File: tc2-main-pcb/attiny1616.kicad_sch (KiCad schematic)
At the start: 16 parts, among them SW2 K2-6639SP-M4SC-04, U1 ATtiny1616-M

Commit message: v0.4.0
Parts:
- removed SW2: K2-6639SP-M4SC-04, cacophony-library:KEY-SMD_4P-L6.0-W6.0-P3.90_K2-6639SP-K4SC-04, symbol cacophony-library:K2-6639SP-O4SC-04
- added SW1: SW_Push, Button_Switch_THT:SW_PUSH_6mm, symbol Switch:SW_Push
- LED1: LCSC (none) -> C2874115; LCSC Part C2874115 -> (none)
- renumbered C56 to C44, R49 to R40, R15 to R46
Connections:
- net ATtiny_SW: now also SW1.1
- net GND: now also SW1.2
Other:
- note added: "140uA when in set_sleep_mode(SLEEP_MODE_PWR_DOWN);"
- note added: "I2C Address 0x25"

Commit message: Small update for v0.4.1
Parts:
- SW1: LCSC (none) -> C4364951
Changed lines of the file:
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@@
+			)
+		)
+		(property "LCSC" "C4364951"
+			(at 204.47 116.84 0)
+			(effects
+				(font
+					(size 1.27 1.27)
+				)
+				(hide yes)
 			)
 		)

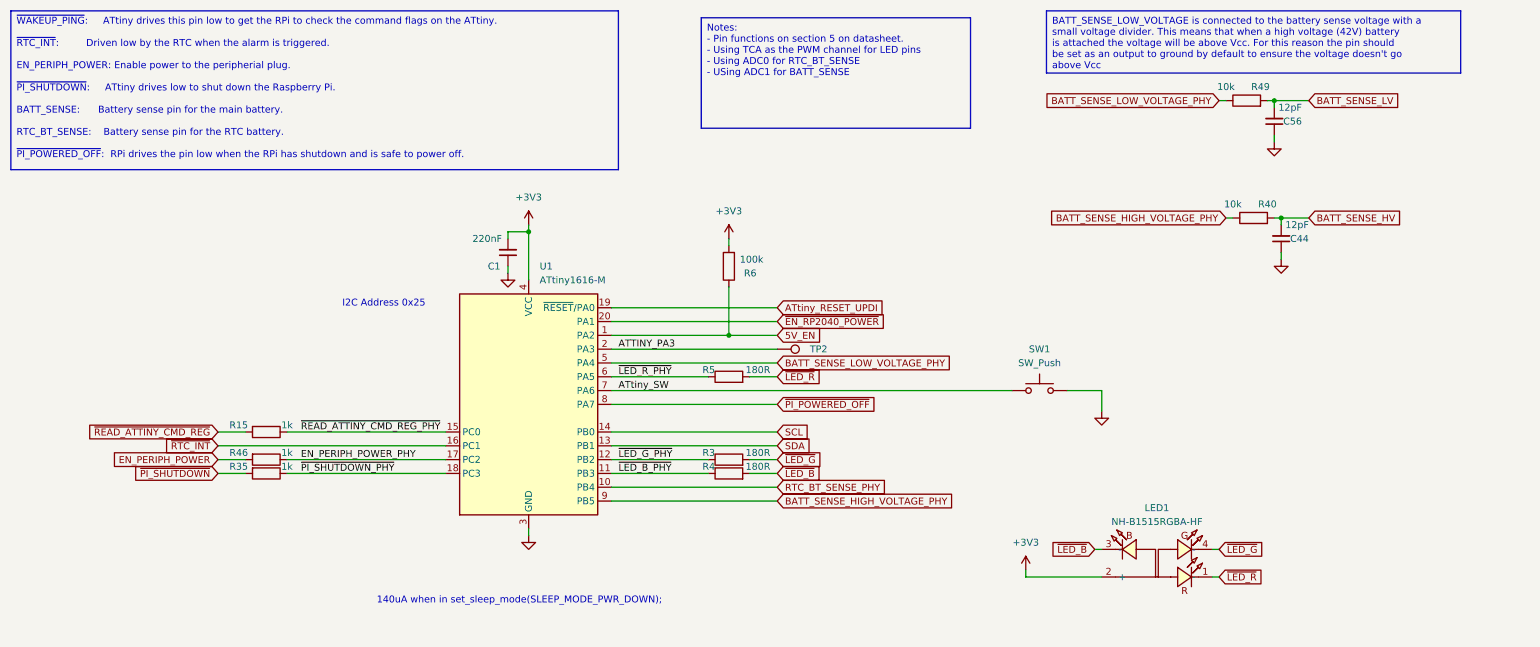
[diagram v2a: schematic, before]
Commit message: Update to use touch sensor
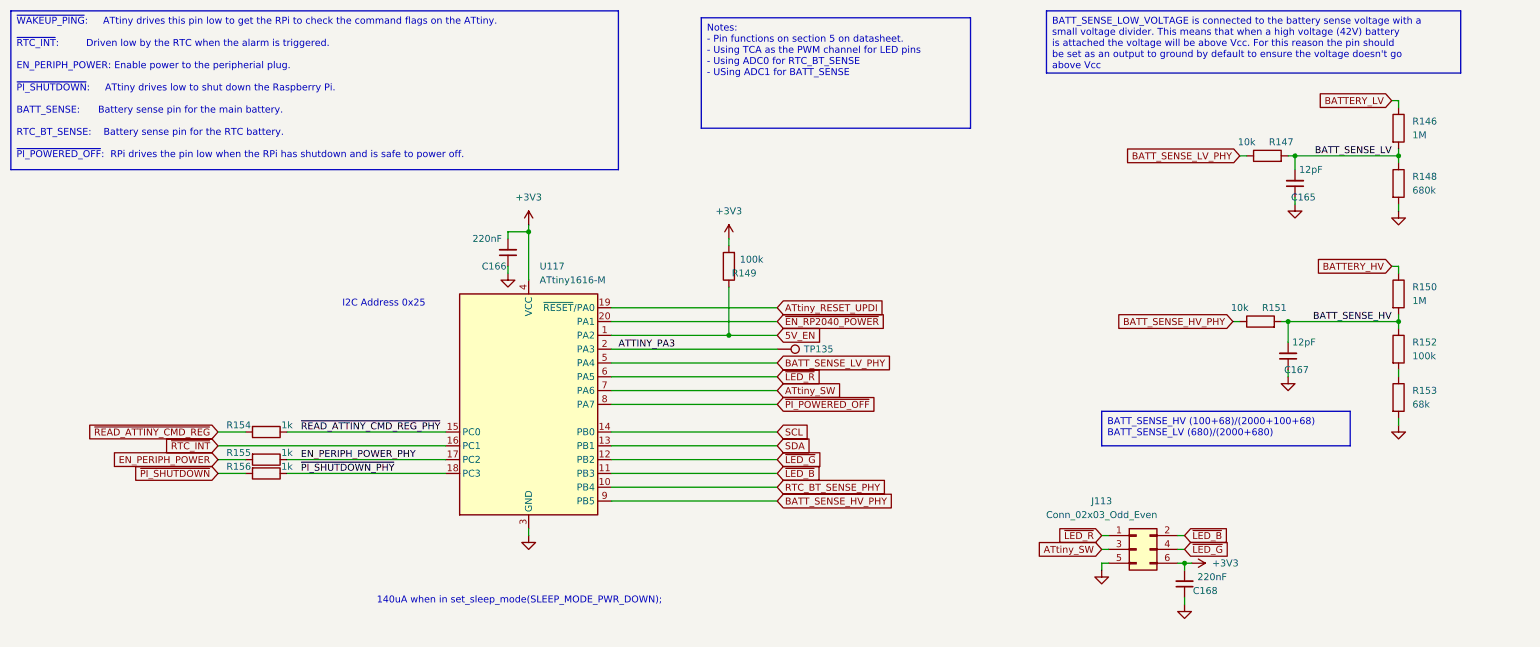
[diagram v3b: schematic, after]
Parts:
- removed LED1: NH-B1515RGBA-HF, cacophony-library:LED-ARRAY-SMD_4P-L1.6-W1.5-TL_NH-B1515RGBA, symbol cacophony-library:NH-B1515RGBA-HF
- removed R3, R4, R5: 180R, Resistor_SMD:R_0402_1005Metric, symbol Device:R
- removed SW1: SW_Push, Button_Switch_THT:SW_PUSH_6mm, symbol Switch:SW_Push
- added C168: 220nF, Capacitor_SMD:C_0402_1005Metric, symbol Device:C_Small
- added J113: Conn_02x03_Odd_Even, cacophony-library:mic-pcb, symbol Connector_Generic:Conn_02x03_Odd_Even
- added R146, R150: 1M, Resistor_SMD:R_0603_1608Metric, symbol Device:R
- added R148: 680k, Resistor_SMD:R_0603_1608Metric, symbol Device:R
- added R152: 100k, Resistor_SMD:R_0402_1005Metric, symbol Device:R
- added R153: 68k, Resistor_SMD:R_0402_1005Metric, symbol Device:R
- renumbered C56 to C165, C1 to C166, C44 to C167, R49 to R147, R6 to R149, R40 to R151, R15 to R154, R46 to R155, R35 to R156, TP2 to TP135, U1 to U117
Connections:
- net ~{LED_B_PHY} is gone; now on net ~{LED_B}: U117.11 (PB3)
- net ~{LED_G_PHY} is gone; now on net ~{LED_G}: U117.12 (PB2)
- net ~{LED_R_PHY} is gone; now on net ~{LED_R}: U117.6 (PA5)
- net +3V3: now also C168.2, J113.6 (Pin_6)
- net ATtiny_SW: now also J113.3 (Pin_3)
- net BATT_SENSE_HV: now also R150.2, R152.1
- net BATT_SENSE_LV: now also R146.2, R148.1
- net GND: now also C168.1, J113.5 (Pin_5), R148.2, R153.2
- net ~{LED_B}: now also J113.2 (Pin_2)
- net ~{LED_G}: now also J113.4 (Pin_4)
- net ~{LED_R}: now also J113.1 (Pin_1)
- net BATT_SENSE_HIGH_VOLTAGE_PHY renamed BATT_SENSE_HV_PHY
- net BATT_SENSE_LOW_VOLTAGE_PHY renamed BATT_SENSE_LV_PHY
- new net: R152.2, R153.1
- new net BATTERY_HV: R150.1
- new net BATTERY_LV: R146.1
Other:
- moved on the sheet: C165, C167, R147, R151

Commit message: Small updates
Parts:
- C165, C167: value 12pF -> 22pF; LCSC C1547 -> C1555
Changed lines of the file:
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@@
 			)
 		)
-		(property "Value" "12pF"
+		(property "Value" "22pF"
 			(at 255.27 107.95 0)
 			(effects
@@
 			)
 		)
-		(property "LCSC" "C1547"
+		(property "LCSC" "C1555"
 			(at 250.19 110.49 0)
 			(effects
@@
 			)
 		)
-		(property "Value" "12pF"
+		(property "Value" "22pF"
 			(at 256.54 76.2 0)
 			(effects
@@
 			)
 		)
-		(property "LCSC" "C1547"
+		(property "LCSC" "C1555"
 			(at 251.46 78.74 0)
 			(effects

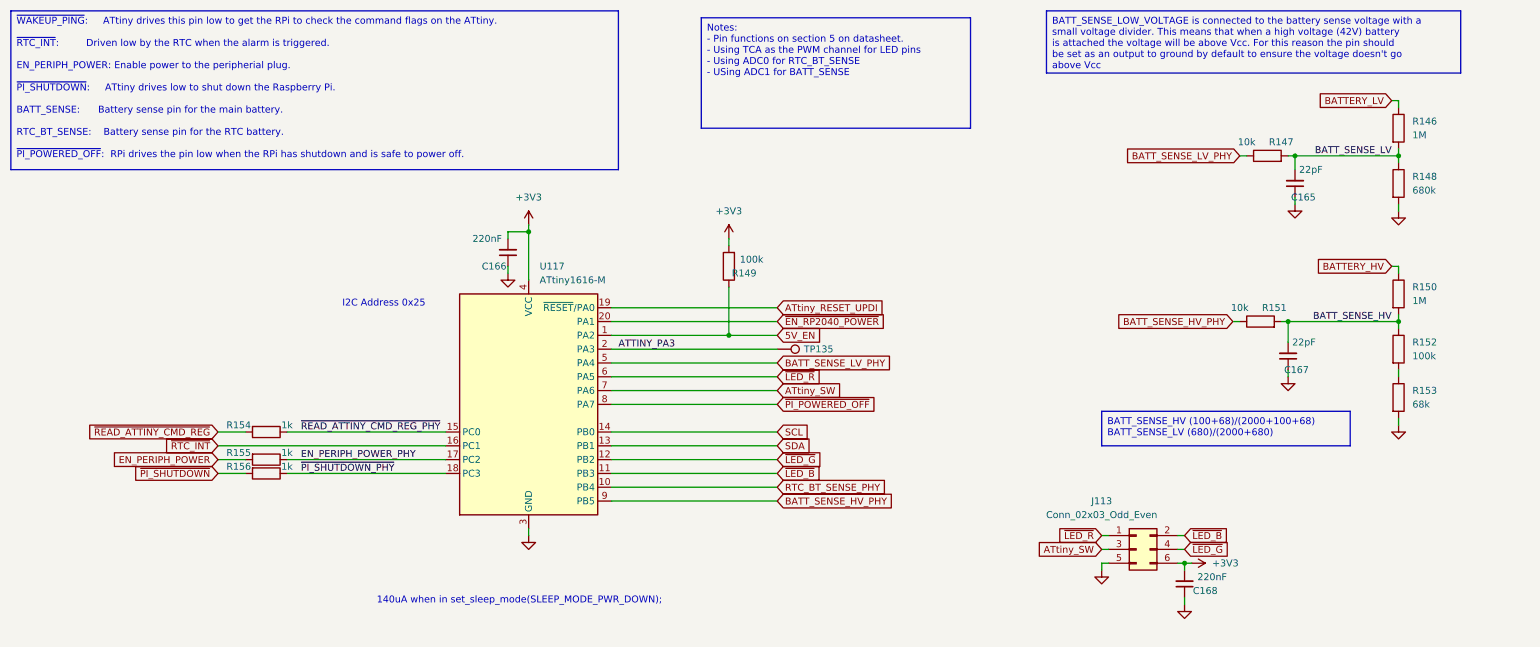
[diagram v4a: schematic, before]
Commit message: Change to through hole connector and add simcard PCB to pannel
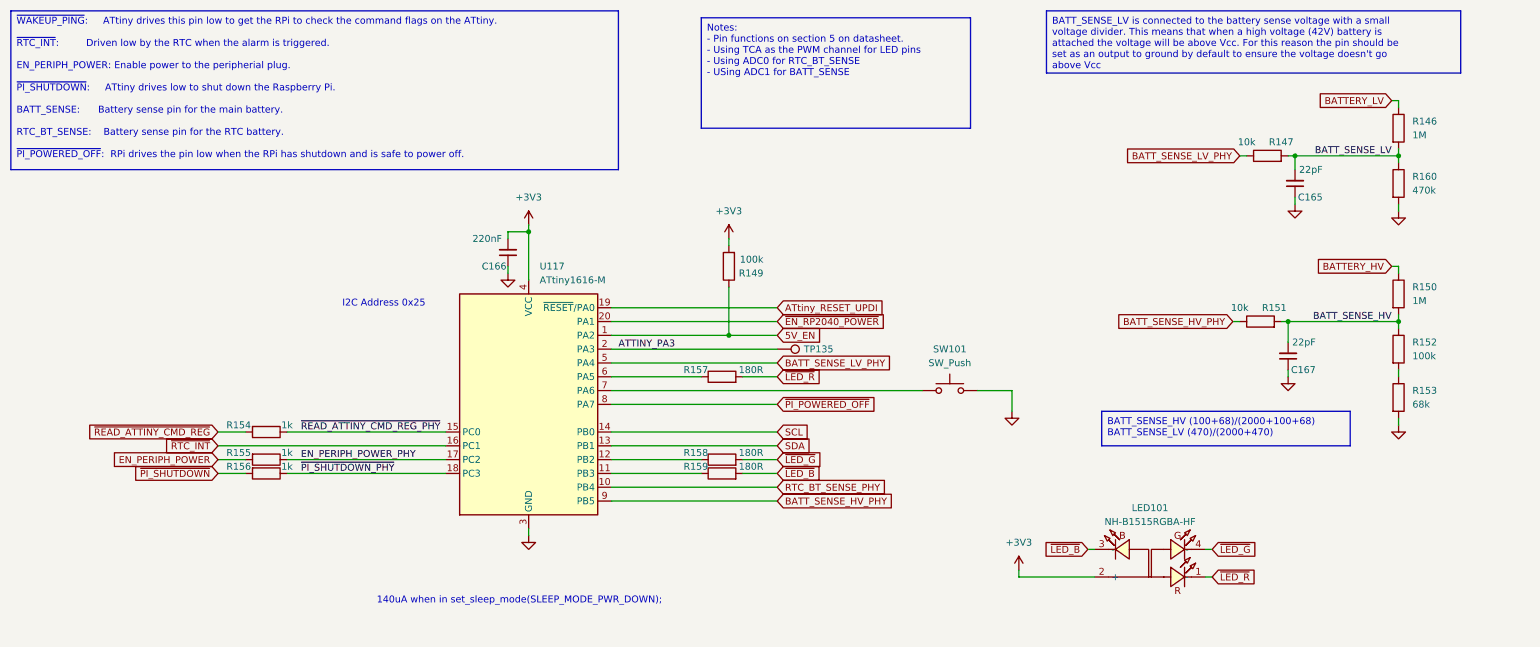
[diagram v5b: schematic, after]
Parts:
- removed C168: 220nF, Capacitor_SMD:C_0402_1005Metric, symbol Device:C_Small
- removed J113: Conn_02x03_Odd_Even, cacophony-library:mic-pcb, symbol Connector_Generic:Conn_02x03_Odd_Even
- removed R148: 680k, Resistor_SMD:R_0603_1608Metric, symbol Device:R
- added LED101: NH-B1515RGBA-HF, cacophony-library:LED-ARRAY-SMD_4P-L1.6-W1.5-TL_NH-B1515RGBA, symbol cacophony-library:NH-B1515RGBA-HF
- added R157, R158, R159: 180R, Resistor_SMD:R_0402_1005Metric, symbol Device:R
- added R160: 470k, Resistor_SMD:R_0402_1005Metric, symbol Device:R
- added SW101: SW_Push, Button_Switch_THT:SW_PUSH_6mm, symbol Switch:SW_Push
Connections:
- net +3V3: now also LED101.2 (+)
- net BATT_SENSE_LV: now also R160.1
- net GND: now also R160.2, SW101.2
- net ~{LED_B}: now also LED101.3 (-), R159.2; no longer U117.11 (PB3)
- net ~{LED_G}: now also LED101.4 (-), R158.2; no longer U117.12 (PB2)
- net ~{LED_R}: now also LED101.1 (-), R157.2; no longer U117.6 (PA5)
- net ATtiny_SW: no longer names the net of U117.7 (PA6)
- net ATtiny_SW: now also SW101.1
- new net: R157.1, U117.6 (PA5)
- new net: R158.1, U117.12 (PB2)
- new net: R159.1, U117.11 (PB3)

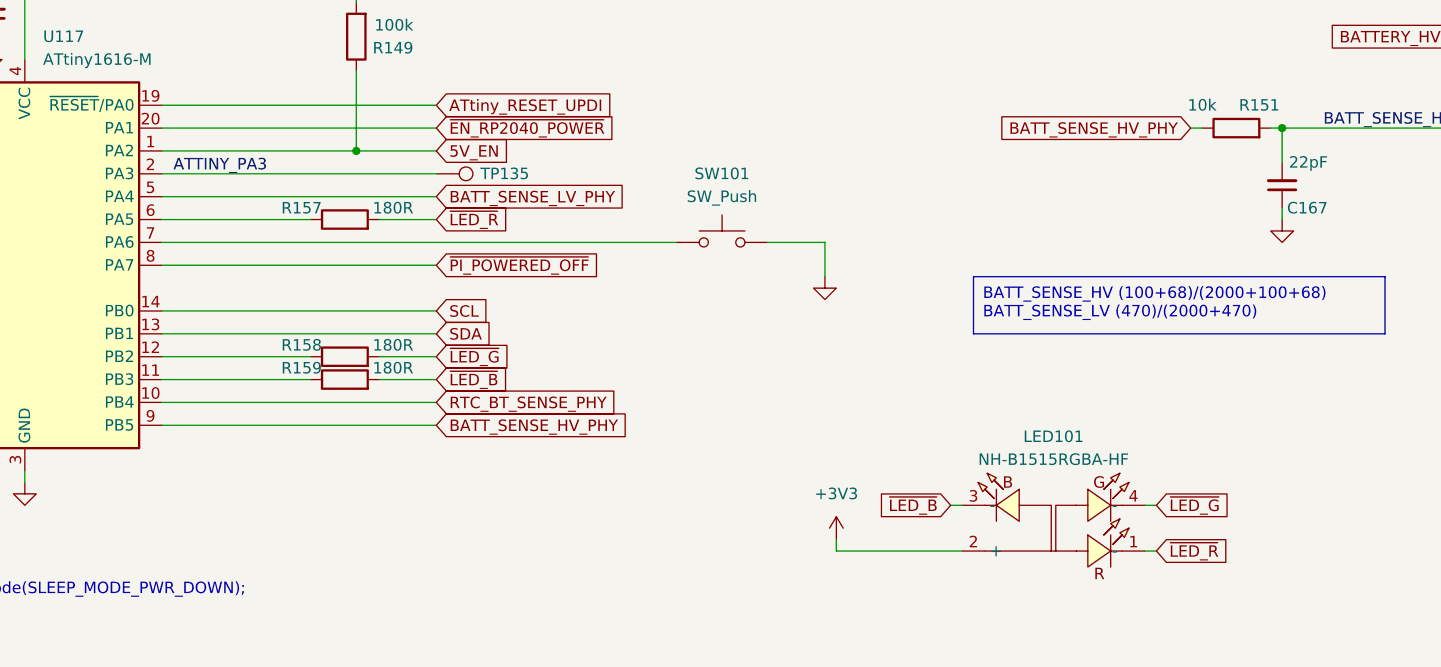
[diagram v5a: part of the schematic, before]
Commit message: v0.7.2 panelise microphone boards
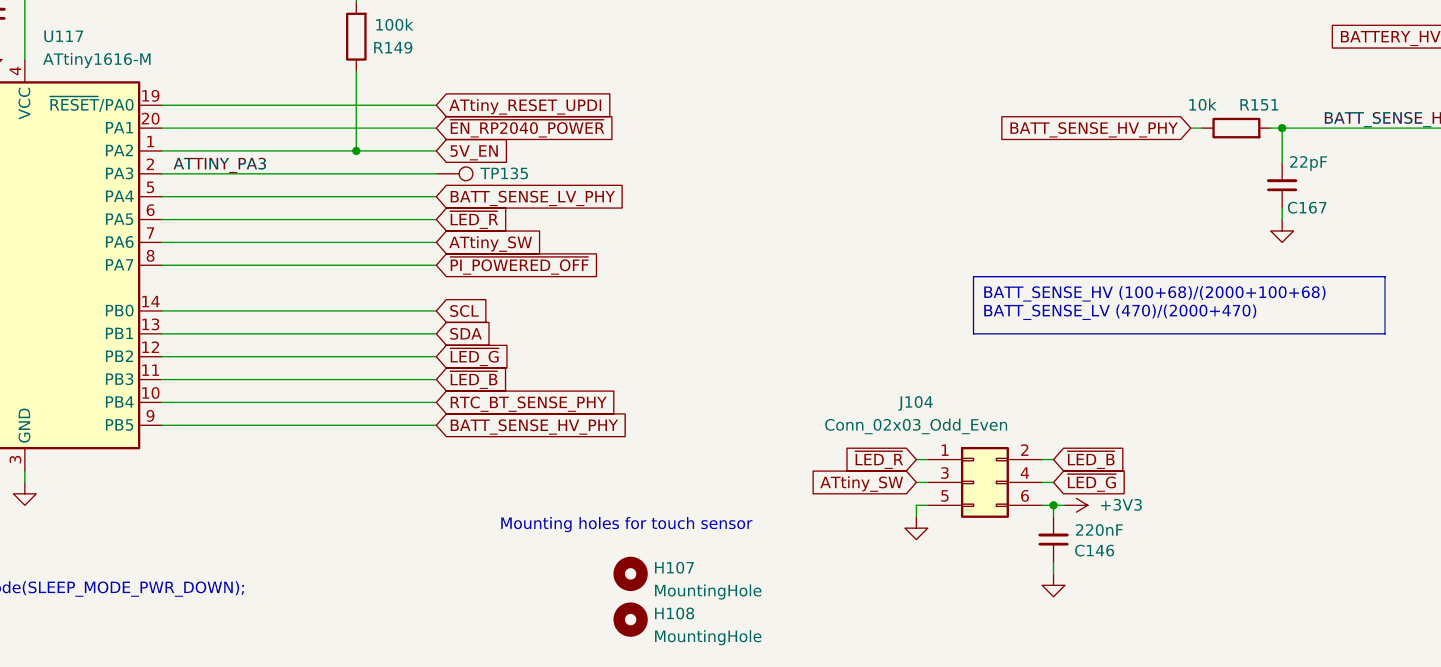
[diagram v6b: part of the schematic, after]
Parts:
- removed LED101: NH-B1515RGBA-HF, cacophony-library:LED-ARRAY-SMD_4P-L1.6-W1.5-TL_NH-B1515RGBA, symbol cacophony-library:NH-B1515RGBA-HF
- removed R157, R158, R159: 180R, Resistor_SMD:R_0402_1005Metric, symbol Device:R
- removed SW101: SW_Push, Button_Switch_THT:SW_PUSH_6mm, symbol Switch:SW_Push
- added C146: 220nF, Capacitor_SMD:C_0402_1005Metric, symbol Device:C_Small
- added H107, H108: MountingHole, cacophony-library:MountingHole_2.2mm_M2, symbol Mechanical:MountingHole
- added J104: Conn_02x03_Odd_Even, cacophony-library:mic-pcb, symbol Connector_Generic:Conn_02x03_Odd_Even
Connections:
- net +3V3: now also C146.2, J104.6 (Pin_6)
- net GND: now also C146.1, J104.5 (Pin_5)
- net ~{LED_B}: now also U117.11 (PB3), J104.2 (Pin_2)
- net ~{LED_G}: now also U117.12 (PB2), J104.4 (Pin_4)
- net ~{LED_R}: now also U117.6 (PA5), J104.1 (Pin_1)
- net ATtiny_SW: now reaches U117.7 (PA6)
- net ATtiny_SW: now also J104.3 (Pin_3)
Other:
- note added: "Mounting holes for touch sensor"
